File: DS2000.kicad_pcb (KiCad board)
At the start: 4 copper layers, 72 x 50 mm, 54 parts, among them J1 USB-C, J2 SWD, J3 USB wire, SW1 MUTE, SW2 DEAFEN, SW3 DISCONNECT, U1 USBLC6-2SC6, U2 AP2112K-3.3, U3 RP2350A, U4 W25Q32JVSS, U5 74AHCT1G125, Y1 12MHz

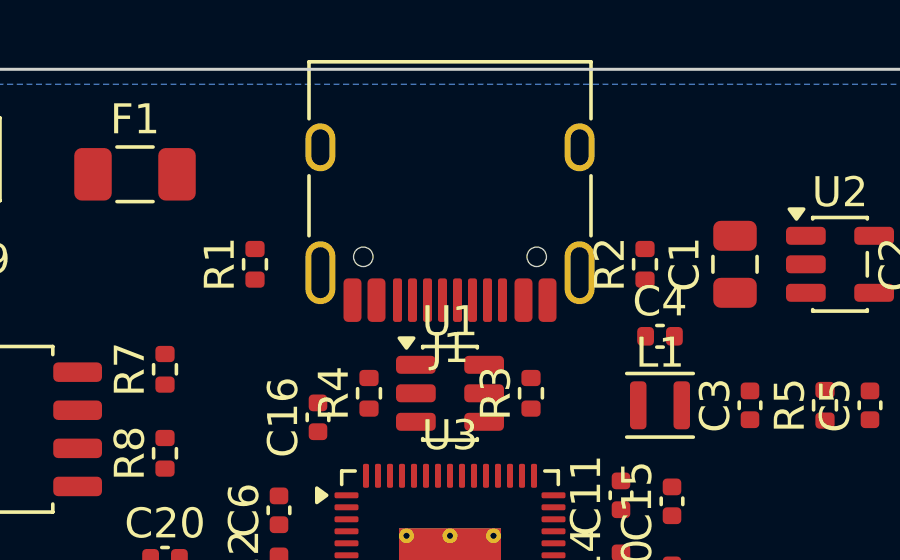
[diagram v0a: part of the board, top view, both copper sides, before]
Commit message: feat: move USB-C underneath and add the missing 3D models
The receptacle moves to the bottom side, still centred on the back edge with its face flush and
opening backwards. The plug and cable now sit low, level with the tray, and the top strip loses
the connector. Its GND pins join the bottom pour solidly: they are too narrow and close together
for thermal spokes.

KiCad's 3D library has no model for the MX switch, the HRO TYPE-C-31-M-12 or the QFN-60 the
footprints point at. tools/3d-models/gen_models.py builds simplified STEP models from datasheet
dimensions (switch with a 1u keycap, receptacle, RP2350A package) into 3dmodels/DS2000.3dshapes,
referenced via ${KIPRJMOD} so they ship with the project. Renders updated.
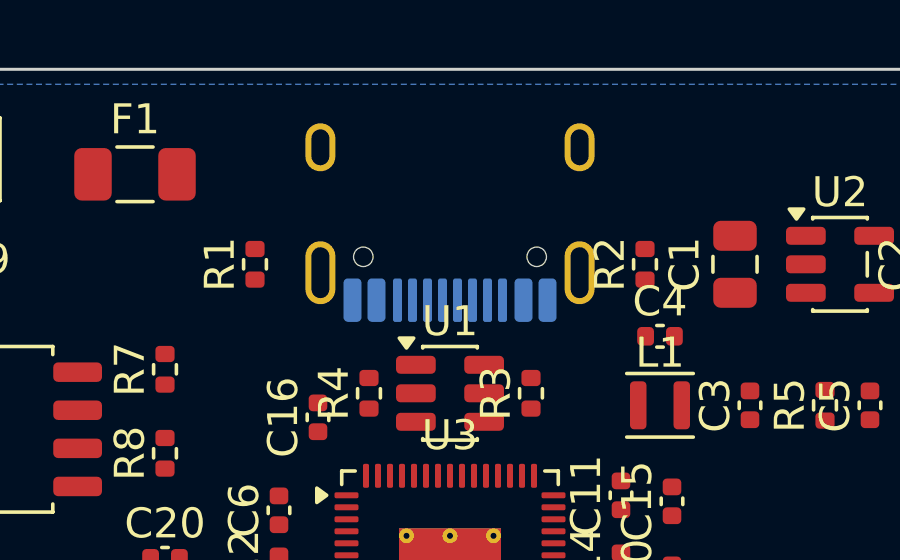
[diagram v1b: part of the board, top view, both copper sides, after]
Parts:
- J1: moved to B.Cu
- turned J1 to 0 degrees

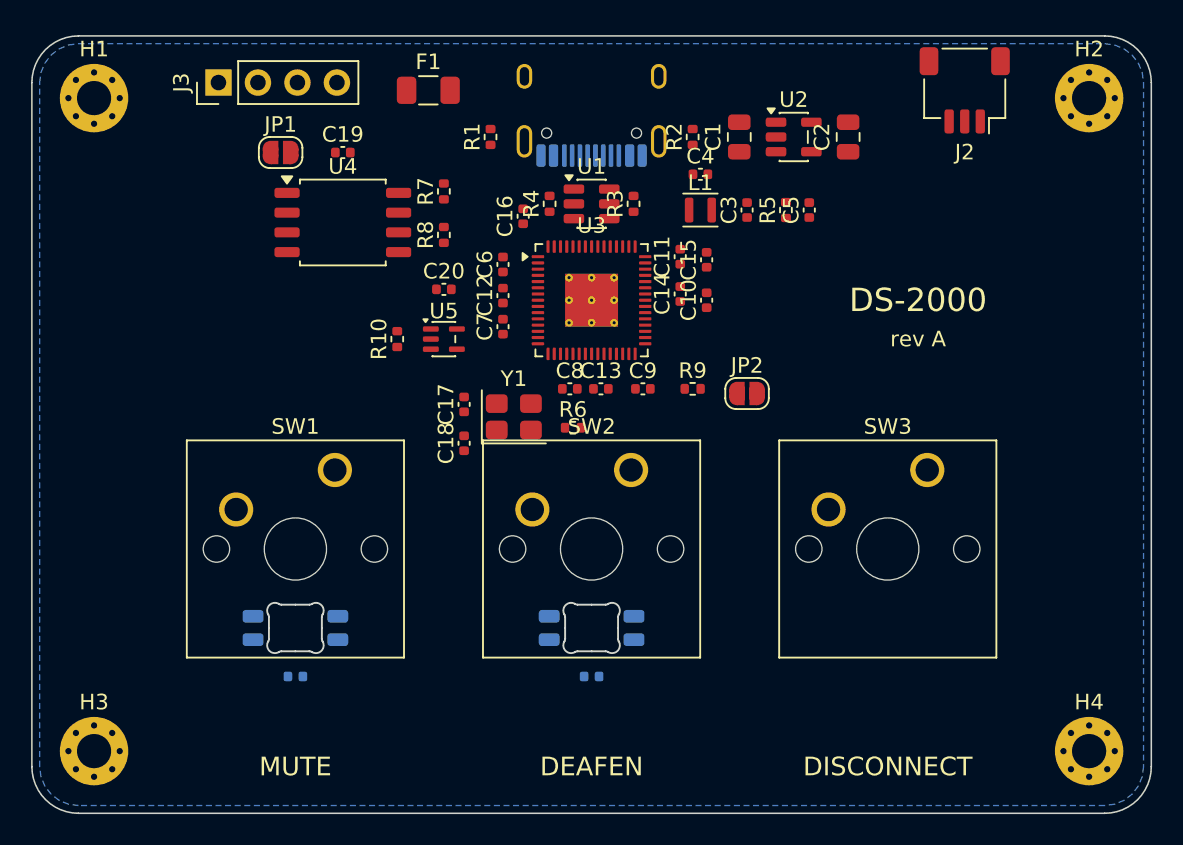
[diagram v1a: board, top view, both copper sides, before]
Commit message: feat: route rev A, shrink the board and move debug underneath
The board is now fully routed: DRC reports no unconnected pads, no clearance or edge errors and
full schematic parity. Only footprint silkscreen overlaps remain.

- 72 x 46 mm, 4 mm shallower: with the USB-C underneath and the SWD connector gone, the strip
  behind the keys needed less depth
- USB-C face now 1.2 mm past the back edge; its front shield tabs keep 0.6 mm of board
- SWD is three bare pads instead of the JST connector, and every debug pad (SWD, BOOT, RST) sits on
  the bottom with its own label
- top-side parts rearranged around the RP2350A pins they serve; decoupling caps in line with their
  pins, USB series resistors between the USB-C pegs straight above D+/D-
- LEDs turned so the data chain runs straight from D1 to D2; bottom GND pour joins pads solidly

Routing is reproducible with tools/pcb-generator/pipeline.py: plane fanout for GND and +3V3 (RP2350A
supply pins tied straight to their capacitors, pins 53/54 sharing one via), then Freerouting for
everything else, with incremental passes. The pipeline writes to build/ and never touches the
committed board, which is now edited by hand.

The core regulator still needs comparing with Raspberry Pi's reference layout before ordering; the
design notes list that and the other checks.
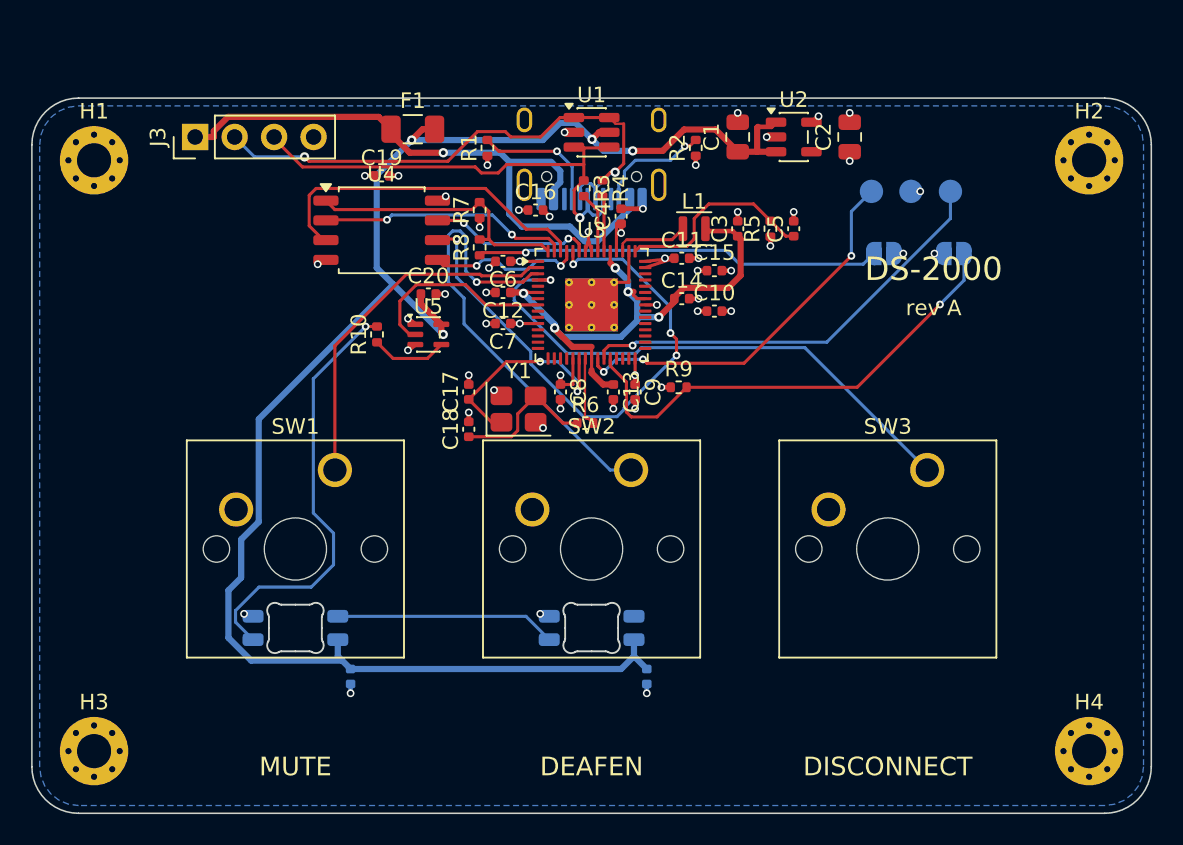
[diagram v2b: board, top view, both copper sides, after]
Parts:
- removed J2: SWD, Connector_JST:JST_SH_SM03B-SRSS-TB_1x03-1MP_P1.00mm_Horizontal
- added TP1: SWCLK, TestPoint:TestPoint_Pad_D1.5mm, B.Cu at (118.0, 77.0)
- added TP2: GND, TestPoint:TestPoint_Pad_D1.5mm, B.Cu at (120.5, 77.0)
- added TP3: SWDIO, TestPoint:TestPoint_Pad_D1.5mm, B.Cu at (123.1, 77.0)
- JP1, JP2: moved to B.Cu
- moved JP1 39.3 mm to (118.8, 81.0), turned to 180 degrees
- moved JP2 16.1 mm to (123.3, 81.0), turned to 180 degrees
- moved C4 5.77 mm to (101.9, 78.6), turned to 90 degrees
- moved U1 4.60 mm to (100.0, 73.2)
- moved H1 4.00 mm to (68.0, 75.0)
- moved H2 4.00 mm to (132.0, 75.0)
- moved J3 3.81 mm to (74.5, 73.5)
- moved C21 3.55 mm to (84.5, 108.2), turned to -90 degrees
- moved C22 3.55 mm to (103.5, 108.2), turned to -90 degrees
- moved R4 3.54 mm to (100.7, 76.8), turned to -90 degrees
- moved R3 3.35 mm to (99.5, 76.8), turned to -90 degrees
- moved C19 2.92 mm to (86.5, 76.0)
- moved J1 2.80 mm to (100.0, 73.5)
- moved F1 2.69 mm to (88.5, 73.0)
- moved R7 2.59 mm to (92.8, 78.2)
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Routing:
- net +5V: track 0.00 -> 108.2 mm, vias 0 -> 4
- net VBUS: track 0.00 -> 41.2 mm, vias 0 -> 1
- net +1V1: track 0.00 -> 36.6 mm, vias 0 -> 5
- net /USB_CONN_DM: track 0.00 -> 36.0 mm, vias 0 -> 2
- net Net-(U3-QSPI_SCLK): track 0.00 -> 35.5 mm, vias 0 -> 4
- net Net-(U3-GPIO2): track 0.00 -> 35.5 mm, vias 0 -> 1
- net /USB_CONN_DP: track 0.00 -> 31.8 mm, vias 0 -> 1
- net /RUN: track 0.00 -> 31.1 mm, vias 0 -> 1
- net Net-(U3-GPIO1): track 0.00 -> 29.5 mm, vias 0 -> 1
- net Net-(U3-SWDIO): track 0.00 -> 28.1 mm, vias 0 -> 1
- net Net-(D1-DIN): track 0.00 -> 27.9 mm, vias 0 -> 1
- net Net-(JP1-B): track 0.00 -> 26.1 mm, vias 0 -> 1
- net +3V3: track 0.00 -> 26.0 mm, vias 0 -> 18
- net GND: track 0.00 -> 25.3 mm, vias 0 -> 36
- net Net-(U3-SWCLK): track 0.00 -> 24.9 mm, vias 0 -> 3
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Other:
- board size 72 x 50 mm -> 72 x 46 mm
- board text added: "BOOT"
- board text added: "CK"
- board text added: "G"
- board text added: "IO"
- board text added: "RST"
- board text added: "SWD"

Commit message: feat: clean up the silkscreen and add the Mechardo Labs mark
Reference designators ran off the board and piled up on each other across the visible face. They
are now hidden (still in the file for assembly drawings), and the USB-C footprint's outline, which
fell past the back edge, moves to the fab layer. The face keeps only the key legends, the debug
labels underneath and the branding. DRC's silkscreen warnings are gone.

The branding sits in the back-left corner, the one area of the face with no top copper:
"DS2000" (no hyphen), "mechardo labs", "rev A", and the Mechardo Labs mark from mechardo3d.xyz.
tools/logo/gen_logo.py traces the site's favicon SVG into DS2000.pretty/Logo_Mechardo_6mm: ENIG
copper whose mask opening leaves the "m" covered, so it reads black on gold. The project footprint
library is registered in fp-lib-table.

tools/pcb-generator/branding.py applies all of this, is safe to re-run on the hand-edited board, and
runs at the end of pipeline.py.
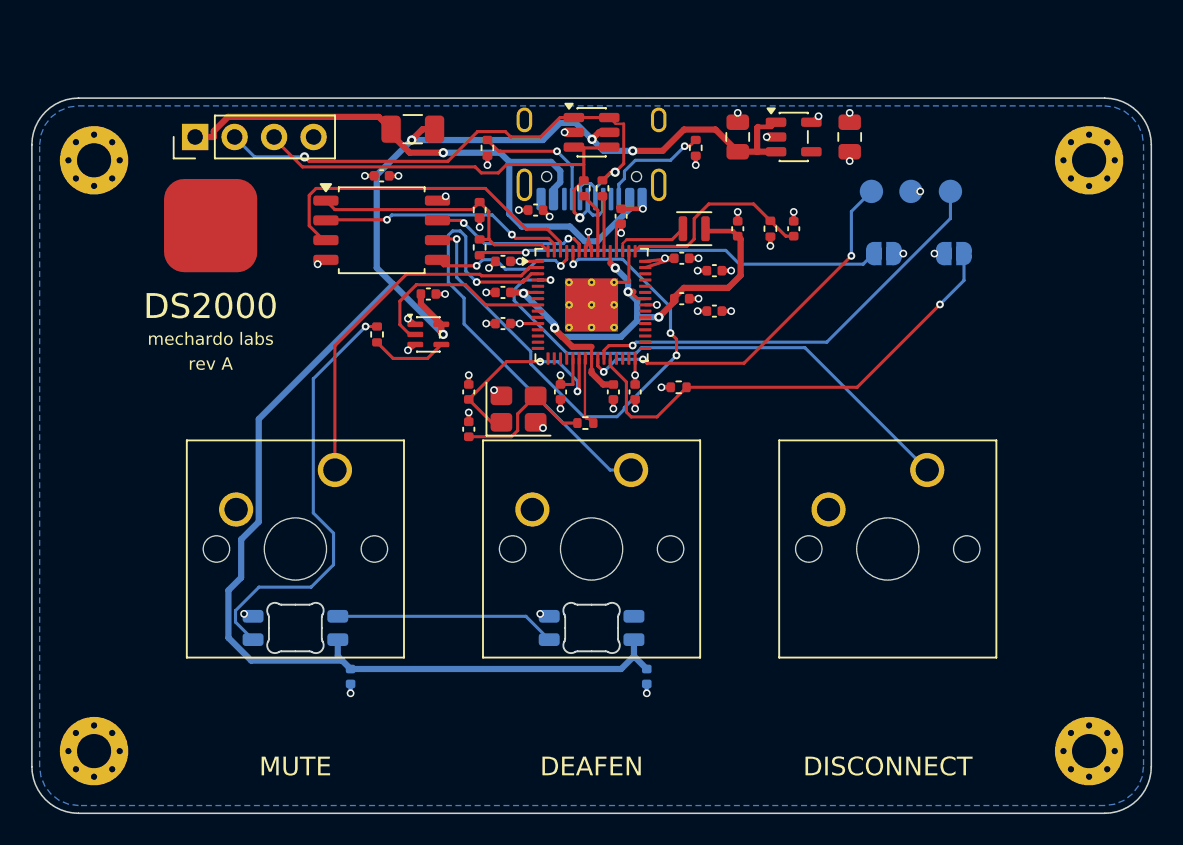
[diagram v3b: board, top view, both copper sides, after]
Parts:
- added LOGO1: Logo_Mechardo_6mm, DS2000:Logo_Mechardo_6mm, F.Cu at (75.5, 79.2)
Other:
- board text added: "DS2000"
- board text added: "mechardo labs"
- board text removed: "DS-2000"

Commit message: feat: top ground pour, tidy references, site typography and a clean logo
- F.Cu gets a GND pour too, so every layer is ground or +3V3 wherever there is no track. Its
  thermals may resolve to one spoke (DS2000.kicad_dru): each top GND pad already has its own via.
- References are visible again, each placed by branding.py at the first spot beside its part that
  clears pads, holes, vias, other text and the board edge. 48 of 51 fit; C6, C11 and R3, in the
  tightest spot around the RP2350A, stay hidden.
- Typography from mechardo3d.xyz instead of KiCad's stroke font: Sora for "DS2000" and "mechardo
  labs", IBM Plex Mono for legends, references and debug labels. The fonts are embedded in the board
  and kept in fonts/ (OFL) for editing. KiCad's TrueType thickness check flags the tapered joins of
  a few glyphs; the main strokes are ~0.16 mm, above JLC's minimum, so the heuristic is relaxed.
- The logo's "m" is one self-overlapping SVG contour; it is now resolved to its nonzero union
  before becoming the mask opening, instead of rendering its overlaps as holes.
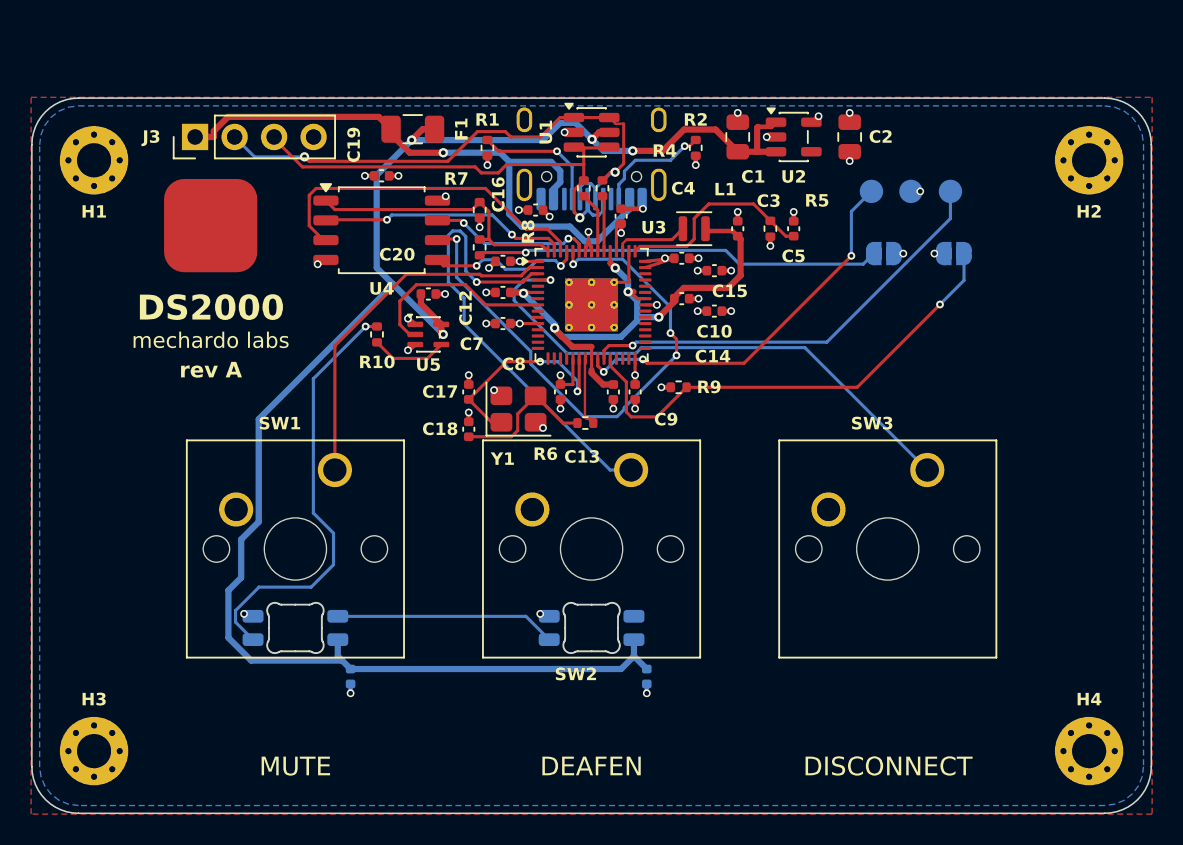
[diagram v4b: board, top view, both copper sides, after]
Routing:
- added copper zone on F.Cu, net GND

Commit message: feat: put the DS2000 logo on the board face
The product logo from mechardo3d.xyz is traced into DS2000.pretty/Logo_DS2000_8.6mm by
tools/logo/gen_ds2000_logo.py: its white lettering becomes silkscreen and its blue arcs ENIG gold,
the board having no blue. The counters of D and 0 are real holes, joined to their outlines by
keyhole cuts since footprint polygons cannot carry holes.

The face now has two blocks in the only two areas without top copper: the DS2000 logo with
"rev A" back-left, and the Mechardo Labs mark (now 5 mm) with "mechardo / labs" back-right. The
"DS2000" text is gone in favour of the logo.
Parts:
- added LOGO2: Logo_DS2000_8.6mm, DS2000:Logo_DS2000_8.6mm, F.Cu at (75.5, 80.8)
- LOGO1: value Logo_Mechardo_6mm -> Logo_Mechardo_5mm; footprint DS2000:Logo_Mechardo_6mm -> DS2000:Logo_Mechardo_5mm
- moved LOGO1 50.5 mm to (126.0, 77.2)
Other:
- board text added: "labs"
- board text added: "mechardo"
- board text removed: "DS2000"
- board text removed: "mechardo labs"
